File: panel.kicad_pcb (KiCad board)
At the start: 2 copper layers, 100 x 96.5 mm, 262 parts, among them J1 JST_SH_SM06B-SRSS-TB_1x06-1MP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, J2 JST_SH_SM04B-SRSS-TB_1x04-1MP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, J4 Conn_01x02, U1 M24C02-FMN

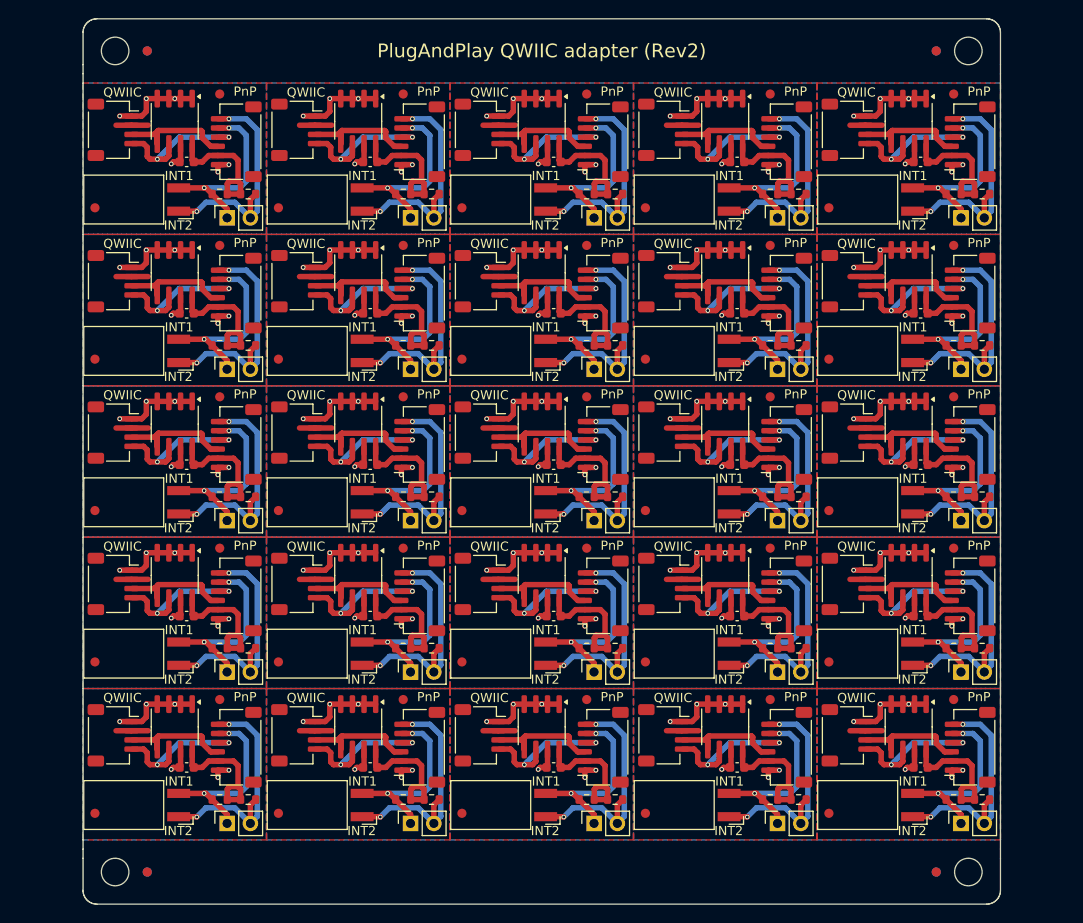
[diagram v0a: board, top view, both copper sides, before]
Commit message: Panel framing on all 4 sides
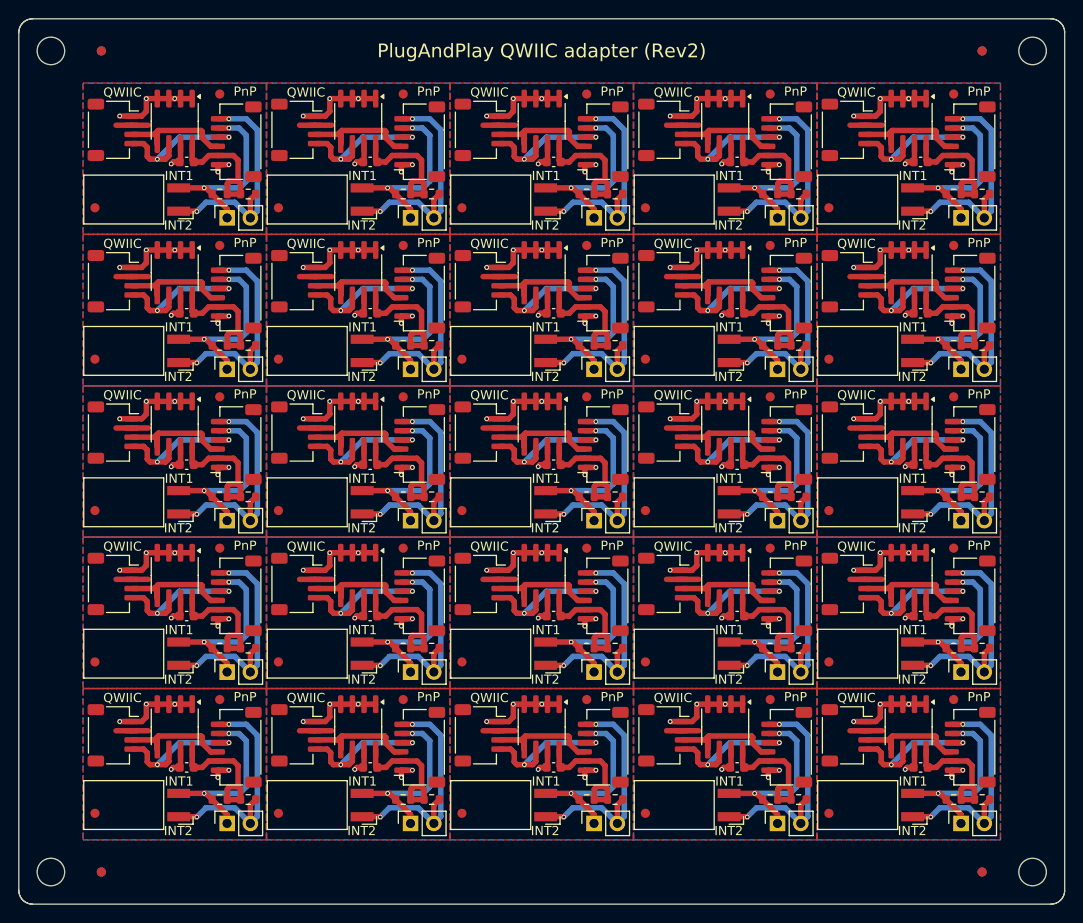
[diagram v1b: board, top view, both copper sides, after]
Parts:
- removed the C1 at (86.3, 101.6)
- removed the C1 at (66.3, 68.6)
- removed the C1 at (66.3, 35.6)
- removed the C1 at (86.3, 68.6)
- removed the C1 at (106.3, 85.1)
- removed the C1 at (86.3, 52.1)
- removed the C1 at (66.3, 101.6)
- removed the C1 at (106.3, 68.6)
- removed the C1 at (66.3, 85.1)
- removed the C1 at (126.3, 35.6)
- removed the C1 at (146.3, 85.1)
- removed the C1 at (86.3, 85.1)
- removed the C1 at (126.3, 101.6)
- removed the C1 at (66.3, 52.1)
- removed the C1 at (106.3, 35.6)
- removed the C1 at (106.3, 52.1)
- removed the C1 at (146.3, 35.6)
- removed the C1 at (126.3, 68.6)
- removed the C1 at (146.3, 52.1)
- removed the C1 at (106.3, 101.6)
- removed the C1 at (146.3, 101.6)
- removed the C1 at (126.3, 85.1)
- removed the C1 at (146.3, 68.6)
- removed the C1 at (126.3, 52.1)
- removed the C1 at (86.3, 35.6)
- removed the J1 at (131.7, 33.4)
- removed the J1 at (91.7, 82.9)
- removed the J1 at (131.7, 82.9)
- removed the J1 at (151.7, 82.9)
- removed the J1 at (131.7, 66.4)
- removed the J1 at (111.7, 99.4)
- removed the J1 at (151.7, 99.4)
- removed the J1 at (71.7, 33.4)
- removed the J1 at (71.7, 49.9)
- removed the J1 at (111.7, 82.9)
- removed the J1 at (71.7, 66.4)
- removed the J1 at (91.7, 66.4)
- removed the J1 at (151.7, 49.9)
- removed the J1 at (71.7, 82.9)
- removed the J1 at (151.7, 33.4)
- removed the J1 at (111.7, 49.9)
- removed the J1 at (111.7, 66.4)
- removed the J1 at (91.7, 33.4)
- removed the J1 at (91.7, 49.9)
- removed the J1 at (111.7, 33.4)
- removed the J1 at (131.7, 99.4)
- removed the J1 at (91.7, 99.4)
- removed the J1 at (151.7, 66.4)
- removed the J1 at (131.7, 49.9)
- removed the J1 at (71.7, 99.4)
- removed the J2 at (138.3, 98.1)
- removed the J2 at (98.3, 48.6)
- removed the J2 at (78.3, 81.6)
- removed the J2 at (78.3, 65.1)
- removed the J2 at (138.3, 48.6)
- removed the J2 at (58.3, 98.1)
- removed the J2 at (118.3, 32.1)
- removed the J2 at (138.3, 65.1)
- removed the J2 at (138.3, 81.6)
- removed the J2 at (118.3, 81.6)
- removed the J2 at (118.3, 65.1)
- removed the J2 at (98.3, 98.1)
- removed the J2 at (118.3, 98.1)
- removed the J2 at (58.3, 65.1)
- removed the J2 at (58.3, 81.6)
- removed the J2 at (98.3, 81.6)
- removed the J2 at (78.3, 48.6)
- removed the J2 at (58.3, 32.1)
- removed the J2 at (138.3, 32.1)
- removed the J2 at (78.3, 98.1)
- removed the J2 at (118.3, 48.6)
- removed the J2 at (58.3, 48.6)
- removed the J2 at (98.3, 32.1)
- removed the J2 at (78.3, 32.1)
- removed the J2 at (98.3, 65.1)
- removed the J3 at (79.9, 87.9)
- removed the J3 at (79.9, 54.9)
- removed the J3 at (139.9, 54.9)
- removed the J3 at (79.9, 104.4)
- removed the J3 at (59.9, 54.9)
- removed the J3 at (99.9, 38.4)
- removed the J3 at (99.9, 71.4)
- removed the J3 at (119.9, 54.9)
- removed the J3 at (119.9, 87.9)
- removed the J3 at (99.9, 54.9)
- removed the J3 at (59.9, 38.4)
- removed the J3 at (79.9, 71.4)
- removed the J3 at (139.9, 38.4)
- removed the J3 at (99.9, 104.4)
- removed the J3 at (139.9, 104.4)
- removed the J3 at (119.9, 104.4)
- removed the J3 at (59.9, 104.4)
- removed the J3 at (139.9, 87.9)
- removed the J3 at (119.9, 71.4)
- removed the J3 at (99.9, 87.9)
- removed the J3 at (59.9, 87.9)
- removed the J3 at (79.9, 38.4)
- removed the J3 at (59.9, 71.4)
- removed the J3 at (139.9, 71.4)
- removed the J3 at (119.9, 38.4)
- removed the J4 at (90.7, 41.7)
- removed the J4 at (70.7, 91.2)
- removed the J4 at (110.7, 41.7)
- removed the J4 at (70.7, 58.2)
- removed the J4 at (130.7, 41.7)
- removed the J4 at (150.7, 107.7)
- removed the J4 at (110.7, 58.2)
- removed the J4 at (110.7, 107.7)
- removed the J4 at (90.7, 74.7)
- removed the J4 at (70.7, 74.7)
- removed the J4 at (90.7, 58.2)
- removed the J4 at (130.7, 91.2)
- removed the J4 at (110.7, 91.2)
- removed the J4 at (150.7, 91.2)
- removed the J4 at (90.7, 107.7)
- removed the J4 at (110.7, 74.7)
- removed the J4 at (70.7, 107.7)
- removed the J4 at (90.7, 91.2)
- removed the J4 at (130.7, 58.2)
- removed the J4 at (130.7, 107.7)
- removed the J4 at (150.7, 41.7)
- removed the J4 at (70.7, 41.7)
- removed the J4 at (130.7, 74.7)
- removed the J4 at (150.7, 58.2)
- removed the J4 at (150.7, 74.7)
- removed the R1 at (113.0, 105.1)
- removed the R1 at (73.0, 105.1)
- removed the R1 at (93.0, 105.1)
- removed the R1 at (93.0, 55.6)
- removed the R1 at (93.0, 39.1)
- removed the R1 at (73.0, 88.6)
- removed the R1 at (73.0, 55.6)
- removed the R1 at (153.0, 88.6)
- removed the R1 at (93.0, 72.1)
- removed the R1 at (113.0, 88.6)
- removed the R1 at (133.0, 105.1)
- removed the R1 at (113.0, 72.1)
- removed the R1 at (153.0, 55.6)
- removed the R1 at (153.0, 105.1)
- removed the R1 at (153.0, 39.1)
- removed the R1 at (133.0, 72.1)
- removed the R1 at (153.0, 72.1)
- removed the R1 at (113.0, 39.1)
- removed the R1 at (133.0, 88.6)
- removed the R1 at (133.0, 39.1)
- removed the R1 at (133.0, 55.6)
- removed the R1 at (73.0, 72.1)
- removed the R1 at (113.0, 55.6)
- removed the R1 at (93.0, 88.6)
- removed the R1 at (73.0, 39.1)
- removed the R2 at (69.9, 72.1)
- removed the R2 at (109.9, 72.1)
- removed the R2 at (89.9, 72.1)
- removed the R2 at (69.9, 39.1)
- removed the R2 at (149.9, 72.1)
- removed the R2 at (129.9, 88.6)
- removed the R2 at (149.9, 105.1)
- removed the R2 at (89.9, 105.1)
- removed the R2 at (89.9, 88.6)
- removed the R2 at (69.9, 88.6)
- removed the R2 at (149.9, 39.1)
- removed the R2 at (129.9, 55.6)
- removed the R2 at (129.9, 105.1)
- removed the R2 at (109.9, 88.6)
- removed the R2 at (109.9, 105.1)
- removed the R2 at (89.9, 55.6)
- removed the R2 at (89.9, 39.1)
- removed the R2 at (69.9, 55.6)
- removed the R2 at (149.9, 55.6)
- removed the R2 at (149.9, 88.6)
- removed the R2 at (129.9, 39.1)
- removed the R2 at (109.9, 55.6)
- removed the R2 at (109.9, 39.1)
- removed the R2 at (69.9, 105.1)
- removed the R2 at (129.9, 72.1)
- removed the REF** at (116.3, 40.6)
- removed the REF** at (129.9, 61.2)
- removed the REF** at (96.3, 90.1)
- removed the REF** at (116.3, 90.1)
- removed the REF** at (76.3, 90.1)
- removed the REF** at (129.9, 44.7)
- removed the REF** at (96.3, 57.1)
- removed the REF** at (96.3, 73.6)
- removed the REF** at (56.3, 106.6)
- removed the REF** at (69.9, 28.2)
- removed the REF** at (116.3, 73.6)
- removed the REF** at (96.3, 106.6)
- removed the REF** at (69.9, 61.2)
- removed the REF** at (136.3, 106.6)
- removed the REF** at (56.3, 90.1)
- removed the REF** at (56.3, 57.1)
- removed the REF** at (76.3, 57.1)
- removed the REF** at (89.9, 94.2)
- removed the REF** at (109.9, 61.2)
- removed the REF** at (109.9, 77.7)
- removed the REF** at (136.3, 40.6)
- removed the REF** at (69.9, 94.2)
- removed the REF** at (76.3, 73.6)
- removed the REF** at (89.9, 77.7)
- removed the REF** at (76.3, 106.6)
- removed the REF** at (149.9, 61.2)
- removed the REF** at (89.9, 28.2)
- removed the REF** at (76.3, 40.6)
- removed the REF** at (136.3, 57.1)
- removed the REF** at (89.9, 44.7)
- removed the REF** at (56.3, 73.6)
- removed the REF** at (69.9, 44.7)
- removed the REF** at (129.9, 94.2)
- removed the REF** at (149.9, 94.2)
- removed the REF** at (149.9, 77.7)
- removed the REF** at (96.3, 40.6)
- removed the REF** at (129.9, 77.7)
- removed the REF** at (149.9, 44.7)
- removed the REF** at (109.9, 94.2)
- removed the REF** at (89.9, 61.2)
- removed the REF** at (56.3, 40.6)
- removed the REF** at (129.9, 28.2)
- removed the REF** at (116.3, 57.1)
- removed the REF** at (136.3, 90.1)
- removed the REF** at (116.3, 106.6)
- removed the REF** at (136.3, 73.6)
- removed the REF** at (109.9, 28.2)
- removed the REF** at (109.9, 44.7)
- removed the REF** at (69.9, 77.7)
- removed the REF** at (149.9, 28.2)
- removed the U1 at (145.0, 80.7)
- removed the U1 at (85.0, 97.2)
- removed the U1 at (125.0, 80.7)
- removed the U1 at (105.0, 47.7)
- removed the U1 at (125.0, 47.7)
- removed the U1 at (65.0, 80.7)
- removed the U1 at (145.0, 47.7)
- removed the U1 at (145.0, 64.2)
- removed the U1 at (145.0, 97.2)
- removed the U1 at (125.0, 31.2)
- removed the U1 at (105.0, 97.2)
- removed the U1 at (85.0, 31.2)
- removed the U1 at (105.0, 31.2)
- removed the U1 at (125.0, 97.2)
- removed the U1 at (85.0, 47.7)
- removed the U1 at (85.0, 64.2)
- removed the U1 at (85.0, 80.7)
- removed the U1 at (65.0, 97.2)
- removed the U1 at (65.0, 47.7)
- removed the U1 at (145.0, 31.2)
- removed the U1 at (65.0, 31.2)
- removed the U1 at (65.0, 64.2)
- removed the U1 at (105.0, 80.7)
- removed the U1 at (105.0, 64.2)
- removed the U1 at (125.0, 64.2)
- added C1: 0.1uF, Capacitor_SMD:C_0603_1608Metric, F.Cu at (86.3, 85.1)
- added C1: 0.1uF, Capacitor_SMD:C_0603_1608Metric, F.Cu at (106.3, 52.1)
- added C1: 0.1uF, Capacitor_SMD:C_0603_1608Metric, F.Cu at (146.3, 68.6)
- added C1: 0.1uF, Capacitor_SMD:C_0603_1608Metric, F.Cu at (126.3, 52.1)
- added C1: 0.1uF, Capacitor_SMD:C_0603_1608Metric, F.Cu at (146.3, 35.6)
- added C1: 0.1uF, Capacitor_SMD:C_0603_1608Metric, F.Cu at (106.3, 101.6)
- added C1: 0.1uF, Capacitor_SMD:C_0603_1608Metric, F.Cu at (126.3, 68.6)
- added C1: 0.1uF, Capacitor_SMD:C_0603_1608Metric, F.Cu at (146.3, 101.6)
- added C1: 0.1uF, Capacitor_SMD:C_0603_1608Metric, F.Cu at (146.3, 52.1)
- added C1: 0.1uF, Capacitor_SMD:C_0603_1608Metric, F.Cu at (106.3, 35.6)
- added C1: 0.1uF, Capacitor_SMD:C_0603_1608Metric, F.Cu at (86.3, 68.6)
- added C1: 0.1uF, Capacitor_SMD:C_0603_1608Metric, F.Cu at (66.3, 101.6)
- added C1: 0.1uF, Capacitor_SMD:C_0603_1608Metric, F.Cu at (66.3, 35.6)
- added C1: 0.1uF, Capacitor_SMD:C_0603_1608Metric, F.Cu at (86.3, 35.6)
- added C1: 0.1uF, Capacitor_SMD:C_0603_1608Metric, F.Cu at (66.3, 85.1)
- added C1: 0.1uF, Capacitor_SMD:C_0603_1608Metric, F.Cu at (126.3, 85.1)
- added C1: 0.1uF, Capacitor_SMD:C_0603_1608Metric, F.Cu at (86.3, 101.6)
- added C1: 0.1uF, Capacitor_SMD:C_0603_1608Metric, F.Cu at (106.3, 68.6)
- added C1: 0.1uF, Capacitor_SMD:C_0603_1608Metric, F.Cu at (66.3, 68.6)
- added C1: 0.1uF, Capacitor_SMD:C_0603_1608Metric, F.Cu at (146.3, 85.1)
- added C1: 0.1uF, Capacitor_SMD:C_0603_1608Metric, F.Cu at (126.3, 35.6)
- added C1: 0.1uF, Capacitor_SMD:C_0603_1608Metric, F.Cu at (66.3, 52.1)
- added C1: 0.1uF, Capacitor_SMD:C_0603_1608Metric, F.Cu at (126.3, 101.6)
- added C1: 0.1uF, Capacitor_SMD:C_0603_1608Metric, F.Cu at (86.3, 52.1)
- added C1: 0.1uF, Capacitor_SMD:C_0603_1608Metric, F.Cu at (106.3, 85.1)
- added J1: JST_SH_SM06B-SRSS-TB_1x06-1MP_P1.00mm_Horizontal, Connector_JST:JST_SH_SM06B-SRSS-TB_1x06-1MP_P1.00mm_Horizontal, F.Cu at (91.7, 66.4)
- added J1: JST_SH_SM06B-SRSS-TB_1x06-1MP_P1.00mm_Horizontal, Connector_JST:JST_SH_SM06B-SRSS-TB_1x06-1MP_P1.00mm_Horizontal, F.Cu at (111.7, 66.4)
- added J1: JST_SH_SM06B-SRSS-TB_1x06-1MP_P1.00mm_Horizontal, Connector_JST:JST_SH_SM06B-SRSS-TB_1x06-1MP_P1.00mm_Horizontal, F.Cu at (111.7, 33.4)
- added J1: JST_SH_SM06B-SRSS-TB_1x06-1MP_P1.00mm_Horizontal, Connector_JST:JST_SH_SM06B-SRSS-TB_1x06-1MP_P1.00mm_Horizontal, F.Cu at (91.7, 99.4)
- added J1: JST_SH_SM06B-SRSS-TB_1x06-1MP_P1.00mm_Horizontal, Connector_JST:JST_SH_SM06B-SRSS-TB_1x06-1MP_P1.00mm_Horizontal, F.Cu at (131.7, 49.9)
- added J1: JST_SH_SM06B-SRSS-TB_1x06-1MP_P1.00mm_Horizontal, Connector_JST:JST_SH_SM06B-SRSS-TB_1x06-1MP_P1.00mm_Horizontal, F.Cu at (131.7, 82.9)
- added J1: JST_SH_SM06B-SRSS-TB_1x06-1MP_P1.00mm_Horizontal, Connector_JST:JST_SH_SM06B-SRSS-TB_1x06-1MP_P1.00mm_Horizontal, F.Cu at (111.7, 82.9)
- added J1: JST_SH_SM06B-SRSS-TB_1x06-1MP_P1.00mm_Horizontal, Connector_JST:JST_SH_SM06B-SRSS-TB_1x06-1MP_P1.00mm_Horizontal, F.Cu at (91.7, 82.9)
- added J1: JST_SH_SM06B-SRSS-TB_1x06-1MP_P1.00mm_Horizontal, Connector_JST:JST_SH_SM06B-SRSS-TB_1x06-1MP_P1.00mm_Horizontal, F.Cu at (111.7, 49.9)
- added J1: JST_SH_SM06B-SRSS-TB_1x06-1MP_P1.00mm_Horizontal, Connector_JST:JST_SH_SM06B-SRSS-TB_1x06-1MP_P1.00mm_Horizontal, F.Cu at (71.7, 99.4)
- added J1: JST_SH_SM06B-SRSS-TB_1x06-1MP_P1.00mm_Horizontal, Connector_JST:JST_SH_SM06B-SRSS-TB_1x06-1MP_P1.00mm_Horizontal, F.Cu at (151.7, 82.9)
- added J1: JST_SH_SM06B-SRSS-TB_1x06-1MP_P1.00mm_Horizontal, Connector_JST:JST_SH_SM06B-SRSS-TB_1x06-1MP_P1.00mm_Horizontal, F.Cu at (151.7, 99.4)
- added J1: JST_SH_SM06B-SRSS-TB_1x06-1MP_P1.00mm_Horizontal, Connector_JST:JST_SH_SM06B-SRSS-TB_1x06-1MP_P1.00mm_Horizontal, F.Cu at (131.7, 66.4)
- added J1: JST_SH_SM06B-SRSS-TB_1x06-1MP_P1.00mm_Horizontal, Connector_JST:JST_SH_SM06B-SRSS-TB_1x06-1MP_P1.00mm_Horizontal, F.Cu at (91.7, 33.4)
- added J1: JST_SH_SM06B-SRSS-TB_1x06-1MP_P1.00mm_Horizontal, Connector_JST:JST_SH_SM06B-SRSS-TB_1x06-1MP_P1.00mm_Horizontal, F.Cu at (151.7, 49.9)
- added J1: JST_SH_SM06B-SRSS-TB_1x06-1MP_P1.00mm_Horizontal, Connector_JST:JST_SH_SM06B-SRSS-TB_1x06-1MP_P1.00mm_Horizontal, F.Cu at (71.7, 82.9)
- added J1: JST_SH_SM06B-SRSS-TB_1x06-1MP_P1.00mm_Horizontal, Connector_JST:JST_SH_SM06B-SRSS-TB_1x06-1MP_P1.00mm_Horizontal, F.Cu at (71.7, 49.9)
- added J1: JST_SH_SM06B-SRSS-TB_1x06-1MP_P1.00mm_Horizontal, Connector_JST:JST_SH_SM06B-SRSS-TB_1x06-1MP_P1.00mm_Horizontal, F.Cu at (71.7, 33.4)
- added J1: JST_SH_SM06B-SRSS-TB_1x06-1MP_P1.00mm_Horizontal, Connector_JST:JST_SH_SM06B-SRSS-TB_1x06-1MP_P1.00mm_Horizontal, F.Cu at (131.7, 99.4)
- added J1: JST_SH_SM06B-SRSS-TB_1x06-1MP_P1.00mm_Horizontal, Connector_JST:JST_SH_SM06B-SRSS-TB_1x06-1MP_P1.00mm_Horizontal, F.Cu at (71.7, 66.4)
- added J1: JST_SH_SM06B-SRSS-TB_1x06-1MP_P1.00mm_Horizontal, Connector_JST:JST_SH_SM06B-SRSS-TB_1x06-1MP_P1.00mm_Horizontal, F.Cu at (91.7, 49.9)
- added J1: JST_SH_SM06B-SRSS-TB_1x06-1MP_P1.00mm_Horizontal, Connector_JST:JST_SH_SM06B-SRSS-TB_1x06-1MP_P1.00mm_Horizontal, F.Cu at (151.7, 66.4)
- added J1: JST_SH_SM06B-SRSS-TB_1x06-1MP_P1.00mm_Horizontal, Connector_JST:JST_SH_SM06B-SRSS-TB_1x06-1MP_P1.00mm_Horizontal, F.Cu at (151.7, 33.4)
- added J1: JST_SH_SM06B-SRSS-TB_1x06-1MP_P1.00mm_Horizontal, Connector_JST:JST_SH_SM06B-SRSS-TB_1x06-1MP_P1.00mm_Horizontal, F.Cu at (111.7, 99.4)
- added J1: JST_SH_SM06B-SRSS-TB_1x06-1MP_P1.00mm_Horizontal, Connector_JST:JST_SH_SM06B-SRSS-TB_1x06-1MP_P1.00mm_Horizontal, F.Cu at (131.7, 33.4)
- added J2: JST_SH_SM04B-SRSS-TB_1x04-1MP_P1.00mm_Horizontal, Connector_JST:JST_SH_SM04B-SRSS-TB_1x04-1MP_P1.00mm_Horizontal, F.Cu at (138.3, 32.1)
- added J2: JST_SH_SM04B-SRSS-TB_1x04-1MP_P1.00mm_Horizontal, Connector_JST:JST_SH_SM04B-SRSS-TB_1x04-1MP_P1.00mm_Horizontal, F.Cu at (58.3, 65.1)
- added J2: JST_SH_SM04B-SRSS-TB_1x04-1MP_P1.00mm_Horizontal, Connector_JST:JST_SH_SM04B-SRSS-TB_1x04-1MP_P1.00mm_Horizontal, F.Cu at (138.3, 81.6)
- added J2: JST_SH_SM04B-SRSS-TB_1x04-1MP_P1.00mm_Horizontal, Connector_JST:JST_SH_SM04B-SRSS-TB_1x04-1MP_P1.00mm_Horizontal, F.Cu at (98.3, 48.6)
- added J2: JST_SH_SM04B-SRSS-TB_1x04-1MP_P1.00mm_Horizontal, Connector_JST:JST_SH_SM04B-SRSS-TB_1x04-1MP_P1.00mm_Horizontal, F.Cu at (138.3, 98.1)
- added J2: JST_SH_SM04B-SRSS-TB_1x04-1MP_P1.00mm_Horizontal, Connector_JST:JST_SH_SM04B-SRSS-TB_1x04-1MP_P1.00mm_Horizontal, F.Cu at (118.3, 81.6)
- added J2: JST_SH_SM04B-SRSS-TB_1x04-1MP_P1.00mm_Horizontal, Connector_JST:JST_SH_SM04B-SRSS-TB_1x04-1MP_P1.00mm_Horizontal, F.Cu at (98.3, 81.6)
- added J2: JST_SH_SM04B-SRSS-TB_1x04-1MP_P1.00mm_Horizontal, Connector_JST:JST_SH_SM04B-SRSS-TB_1x04-1MP_P1.00mm_Horizontal, F.Cu at (98.3, 98.1)
- added J2: JST_SH_SM04B-SRSS-TB_1x04-1MP_P1.00mm_Horizontal, Connector_JST:JST_SH_SM04B-SRSS-TB_1x04-1MP_P1.00mm_Horizontal, F.Cu at (98.3, 65.1)
- added J2: JST_SH_SM04B-SRSS-TB_1x04-1MP_P1.00mm_Horizontal, Connector_JST:JST_SH_SM04B-SRSS-TB_1x04-1MP_P1.00mm_Horizontal, F.Cu at (138.3, 65.1)
- added J2: JST_SH_SM04B-SRSS-TB_1x04-1MP_P1.00mm_Horizontal, Connector_JST:JST_SH_SM04B-SRSS-TB_1x04-1MP_P1.00mm_Horizontal, F.Cu at (78.3, 32.1)
- added J2: JST_SH_SM04B-SRSS-TB_1x04-1MP_P1.00mm_Horizontal, Connector_JST:JST_SH_SM04B-SRSS-TB_1x04-1MP_P1.00mm_Horizontal, F.Cu at (98.3, 32.1)
- added J2: JST_SH_SM04B-SRSS-TB_1x04-1MP_P1.00mm_Horizontal, Connector_JST:JST_SH_SM04B-SRSS-TB_1x04-1MP_P1.00mm_Horizontal, F.Cu at (58.3, 32.1)
- added J2: JST_SH_SM04B-SRSS-TB_1x04-1MP_P1.00mm_Horizontal, Connector_JST:JST_SH_SM04B-SRSS-TB_1x04-1MP_P1.00mm_Horizontal, F.Cu at (78.3, 65.1)
- added J2: JST_SH_SM04B-SRSS-TB_1x04-1MP_P1.00mm_Horizontal, Connector_JST:JST_SH_SM04B-SRSS-TB_1x04-1MP_P1.00mm_Horizontal, F.Cu at (78.3, 48.6)
- added J2: JST_SH_SM04B-SRSS-TB_1x04-1MP_P1.00mm_Horizontal, Connector_JST:JST_SH_SM04B-SRSS-TB_1x04-1MP_P1.00mm_Horizontal, F.Cu at (118.3, 48.6)
- added J2: JST_SH_SM04B-SRSS-TB_1x04-1MP_P1.00mm_Horizontal, Connector_JST:JST_SH_SM04B-SRSS-TB_1x04-1MP_P1.00mm_Horizontal, F.Cu at (58.3, 98.1)
- added J2: JST_SH_SM04B-SRSS-TB_1x04-1MP_P1.00mm_Horizontal, Connector_JST:JST_SH_SM04B-SRSS-TB_1x04-1MP_P1.00mm_Horizontal, F.Cu at (118.3, 65.1)
- added J2: JST_SH_SM04B-SRSS-TB_1x04-1MP_P1.00mm_Horizontal, Connector_JST:JST_SH_SM04B-SRSS-TB_1x04-1MP_P1.00mm_Horizontal, F.Cu at (78.3, 81.6)
- added J2: JST_SH_SM04B-SRSS-TB_1x04-1MP_P1.00mm_Horizontal, Connector_JST:JST_SH_SM04B-SRSS-TB_1x04-1MP_P1.00mm_Horizontal, F.Cu at (78.3, 98.1)
- added J2: JST_SH_SM04B-SRSS-TB_1x04-1MP_P1.00mm_Horizontal, Connector_JST:JST_SH_SM04B-SRSS-TB_1x04-1MP_P1.00mm_Horizontal, F.Cu at (118.3, 98.1)
- added J2: JST_SH_SM04B-SRSS-TB_1x04-1MP_P1.00mm_Horizontal, Connector_JST:JST_SH_SM04B-SRSS-TB_1x04-1MP_P1.00mm_Horizontal, F.Cu at (138.3, 48.6)
- added J2: JST_SH_SM04B-SRSS-TB_1x04-1MP_P1.00mm_Horizontal, Connector_JST:JST_SH_SM04B-SRSS-TB_1x04-1MP_P1.00mm_Horizontal, F.Cu at (118.3, 32.1)
- added J2: JST_SH_SM04B-SRSS-TB_1x04-1MP_P1.00mm_Horizontal, Connector_JST:JST_SH_SM04B-SRSS-TB_1x04-1MP_P1.00mm_Horizontal, F.Cu at (58.3, 48.6)
- added J2: JST_SH_SM04B-SRSS-TB_1x04-1MP_P1.00mm_Horizontal, Connector_JST:JST_SH_SM04B-SRSS-TB_1x04-1MP_P1.00mm_Horizontal, F.Cu at (58.3, 81.6)
- added J3: ~, Library:PinHeader_1x02_P2.54mm_Horizontal_SMD, F.Cu at (79.9, 54.9)
- added J3: ~, Library:PinHeader_1x02_P2.54mm_Horizontal_SMD, F.Cu at (139.9, 104.4)
- added J3: ~, Library:PinHeader_1x02_P2.54mm_Horizontal_SMD, F.Cu at (119.9, 54.9)
- added J3: ~, Library:PinHeader_1x02_P2.54mm_Horizontal_SMD, F.Cu at (59.9, 38.4)
- added J3: ~, Library:PinHeader_1x02_P2.54mm_Horizontal_SMD, F.Cu at (99.9, 104.4)
- added J3: ~, Library:PinHeader_1x02_P2.54mm_Horizontal_SMD, F.Cu at (99.9, 71.4)
- added J3: ~, Library:PinHeader_1x02_P2.54mm_Horizontal_SMD, F.Cu at (79.9, 104.4)
- added J3: ~, Library:PinHeader_1x02_P2.54mm_Horizontal_SMD, F.Cu at (99.9, 87.9)
- added J3: ~, Library:PinHeader_1x02_P2.54mm_Horizontal_SMD, F.Cu at (139.9, 38.4)
- added J3: ~, Library:PinHeader_1x02_P2.54mm_Horizontal_SMD, F.Cu at (59.9, 54.9)
- added J3: ~, Library:PinHeader_1x02_P2.54mm_Horizontal_SMD, F.Cu at (59.9, 71.4)
- added J3: ~, Library:PinHeader_1x02_P2.54mm_Horizontal_SMD, F.Cu at (119.9, 87.9)
- added J3: ~, Library:PinHeader_1x02_P2.54mm_Horizontal_SMD, F.Cu at (119.9, 38.4)
- added J3: ~, Library:PinHeader_1x02_P2.54mm_Horizontal_SMD, F.Cu at (59.9, 87.9)
- added J3: ~, Library:PinHeader_1x02_P2.54mm_Horizontal_SMD, F.Cu at (139.9, 54.9)
- added J3: ~, Library:PinHeader_1x02_P2.54mm_Horizontal_SMD, F.Cu at (79.9, 71.4)
- added J3: ~, Library:PinHeader_1x02_P2.54mm_Horizontal_SMD, F.Cu at (99.9, 38.4)
- added J3: ~, Library:PinHeader_1x02_P2.54mm_Horizontal_SMD, F.Cu at (99.9, 54.9)
- added J3: ~, Library:PinHeader_1x02_P2.54mm_Horizontal_SMD, F.Cu at (79.9, 87.9)
- added J3: ~, Library:PinHeader_1x02_P2.54mm_Horizontal_SMD, F.Cu at (79.9, 38.4)
- added J3: ~, Library:PinHeader_1x02_P2.54mm_Horizontal_SMD, F.Cu at (119.9, 71.4)
- added J3: ~, Library:PinHeader_1x02_P2.54mm_Horizontal_SMD, F.Cu at (119.9, 104.4)
- added J3: ~, Library:PinHeader_1x02_P2.54mm_Horizontal_SMD, F.Cu at (139.9, 87.9)
- added J3: ~, Library:PinHeader_1x02_P2.54mm_Horizontal_SMD, F.Cu at (139.9, 71.4)
- added J3: ~, Library:PinHeader_1x02_P2.54mm_Horizontal_SMD, F.Cu at (59.9, 104.4)
- added J4: Conn_01x02, Connector_PinSocket_2.54mm:PinSocket_1x02_P2.54mm_Vertical, F.Cu at (110.7, 58.2)
- added J4: Conn_01x02, Connector_PinSocket_2.54mm:PinSocket_1x02_P2.54mm_Vertical, F.Cu at (90.7, 58.2)
- added J4: Conn_01x02, Connector_PinSocket_2.54mm:PinSocket_1x02_P2.54mm_Vertical, F.Cu at (130.7, 91.2)
- added J4: Conn_01x02, Connector_PinSocket_2.54mm:PinSocket_1x02_P2.54mm_Vertical, F.Cu at (90.7, 74.7)
- added J4: Conn_01x02, Connector_PinSocket_2.54mm:PinSocket_1x02_P2.54mm_Vertical, F.Cu at (90.7, 41.7)
- added J4: Conn_01x02, Connector_PinSocket_2.54mm:PinSocket_1x02_P2.54mm_Vertical, F.Cu at (70.7, 91.2)
- added J4: Conn_01x02, Connector_PinSocket_2.54mm:PinSocket_1x02_P2.54mm_Vertical, F.Cu at (110.7, 107.7)
- added J4: Conn_01x02, Connector_PinSocket_2.54mm:PinSocket_1x02_P2.54mm_Vertical, F.Cu at (150.7, 107.7)
- added J4: Conn_01x02, Connector_PinSocket_2.54mm:PinSocket_1x02_P2.54mm_Vertical, F.Cu at (150.7, 91.2)
- added J4: Conn_01x02, Connector_PinSocket_2.54mm:PinSocket_1x02_P2.54mm_Vertical, F.Cu at (70.7, 74.7)
- added J4: Conn_01x02, Connector_PinSocket_2.54mm:PinSocket_1x02_P2.54mm_Vertical, F.Cu at (70.7, 107.7)
- added J4: Conn_01x02, Connector_PinSocket_2.54mm:PinSocket_1x02_P2.54mm_Vertical, F.Cu at (110.7, 91.2)
- added J4: Conn_01x02, Connector_PinSocket_2.54mm:PinSocket_1x02_P2.54mm_Vertical, F.Cu at (110.7, 74.7)
- added J4: Conn_01x02, Connector_PinSocket_2.54mm:PinSocket_1x02_P2.54mm_Vertical, F.Cu at (130.7, 74.7)
- added J4: Conn_01x02, Connector_PinSocket_2.54mm:PinSocket_1x02_P2.54mm_Vertical, F.Cu at (130.7, 41.7)
- added J4: Conn_01x02, Connector_PinSocket_2.54mm:PinSocket_1x02_P2.54mm_Vertical, F.Cu at (130.7, 107.7)
- added J4: Conn_01x02, Connector_PinSocket_2.54mm:PinSocket_1x02_P2.54mm_Vertical, F.Cu at (90.7, 91.2)
- added J4: Conn_01x02, Connector_PinSocket_2.54mm:PinSocket_1x02_P2.54mm_Vertical, F.Cu at (70.7, 58.2)
- added J4: Conn_01x02, Connector_PinSocket_2.54mm:PinSocket_1x02_P2.54mm_Vertical, F.Cu at (150.7, 41.7)
- added J4: Conn_01x02, Connector_PinSocket_2.54mm:PinSocket_1x02_P2.54mm_Vertical, F.Cu at (150.7, 74.7)
- added J4: Conn_01x02, Connector_PinSocket_2.54mm:PinSocket_1x02_P2.54mm_Vertical, F.Cu at (70.7, 41.7)
- added J4: Conn_01x02, Connector_PinSocket_2.54mm:PinSocket_1x02_P2.54mm_Vertical, F.Cu at (110.7, 41.7)
- added J4: Conn_01x02, Connector_PinSocket_2.54mm:PinSocket_1x02_P2.54mm_Vertical, F.Cu at (90.7, 107.7)
- added J4: Conn_01x02, Connector_PinSocket_2.54mm:PinSocket_1x02_P2.54mm_Vertical, F.Cu at (130.7, 58.2)
- added J4: Conn_01x02, Connector_PinSocket_2.54mm:PinSocket_1x02_P2.54mm_Vertical, F.Cu at (150.7, 58.2)
- added R1: 10K, Resistor_SMD:R_0603_1608Metric, F.Cu at (113.0, 105.1)
- added R1: 10K, Resistor_SMD:R_0603_1608Metric, F.Cu at (73.0, 39.1)
- added R1: 10K, Resistor_SMD:R_0603_1608Metric, F.Cu at (93.0, 55.6)
- added R1: 10K, Resistor_SMD:R_0603_1608Metric, F.Cu at (73.0, 88.6)
- added R1: 10K, Resistor_SMD:R_0603_1608Metric, F.Cu at (153.0, 55.6)
- added R1: 10K, Resistor_SMD:R_0603_1608Metric, F.Cu at (113.0, 55.6)
- added R1: 10K, Resistor_SMD:R_0603_1608Metric, F.Cu at (73.0, 72.1)
- added R1: 10K, Resistor_SMD:R_0603_1608Metric, F.Cu at (153.0, 72.1)
- added R1: 10K, Resistor_SMD:R_0603_1608Metric, F.Cu at (113.0, 88.6)
- added R1: 10K, Resistor_SMD:R_0603_1608Metric, F.Cu at (113.0, 72.1)
- added R1: 10K, Resistor_SMD:R_0603_1608Metric, F.Cu at (133.0, 39.1)
- added R1: 10K, Resistor_SMD:R_0603_1608Metric, F.Cu at (153.0, 88.6)
- added R1: 10K, Resistor_SMD:R_0603_1608Metric, F.Cu at (133.0, 72.1)
- added R1: 10K, Resistor_SMD:R_0603_1608Metric, F.Cu at (133.0, 55.6)
- added R1: 10K, Resistor_SMD:R_0603_1608Metric, F.Cu at (73.0, 105.1)
- added R1: 10K, Resistor_SMD:R_0603_1608Metric, F.Cu at (73.0, 55.6)
- added R1: 10K, Resistor_SMD:R_0603_1608Metric, F.Cu at (93.0, 72.1)
- added R1: 10K, Resistor_SMD:R_0603_1608Metric, F.Cu at (93.0, 88.6)
- added R1: 10K, Resistor_SMD:R_0603_1608Metric, F.Cu at (93.0, 39.1)
- added R1: 10K, Resistor_SMD:R_0603_1608Metric, F.Cu at (93.0, 105.1)
- added R1: 10K, Resistor_SMD:R_0603_1608Metric, F.Cu at (153.0, 39.1)
- added R1: 10K, Resistor_SMD:R_0603_1608Metric, F.Cu at (133.0, 105.1)
- added R1: 10K, Resistor_SMD:R_0603_1608Metric, F.Cu at (113.0, 39.1)
- added R1: 10K, Resistor_SMD:R_0603_1608Metric, F.Cu at (153.0, 105.1)
- added R1: 10K, Resistor_SMD:R_0603_1608Metric, F.Cu at (133.0, 88.6)
- added R2: 10K, Resistor_SMD:R_0603_1608Metric, F.Cu at (109.9, 88.6)
- added R2: 10K, Resistor_SMD:R_0603_1608Metric, F.Cu at (149.9, 39.1)
- added R2: 10K, Resistor_SMD:R_0603_1608Metric, F.Cu at (149.9, 88.6)
- added R2: 10K, Resistor_SMD:R_0603_1608Metric, F.Cu at (69.9, 88.6)
- added R2: 10K, Resistor_SMD:R_0603_1608Metric, F.Cu at (69.9, 105.1)
- added R2: 10K, Resistor_SMD:R_0603_1608Metric, F.Cu at (129.9, 105.1)
- added R2: 10K, Resistor_SMD:R_0603_1608Metric, F.Cu at (129.9, 39.1)
- added R2: 10K, Resistor_SMD:R_0603_1608Metric, F.Cu at (89.9, 105.1)
- added R2: 10K, Resistor_SMD:R_0603_1608Metric, F.Cu at (129.9, 88.6)
- added R2: 10K, Resistor_SMD:R_0603_1608Metric, F.Cu at (89.9, 55.6)
- added R2: 10K, Resistor_SMD:R_0603_1608Metric, F.Cu at (149.9, 55.6)
- added R2: 10K, Resistor_SMD:R_0603_1608Metric, F.Cu at (149.9, 72.1)
- added R2: 10K, Resistor_SMD:R_0603_1608Metric, F.Cu at (109.9, 39.1)
- added R2: 10K, Resistor_SMD:R_0603_1608Metric, F.Cu at (89.9, 39.1)
- added R2: 10K, Resistor_SMD:R_0603_1608Metric, F.Cu at (69.9, 55.6)
- added R2: 10K, Resistor_SMD:R_0603_1608Metric, F.Cu at (129.9, 55.6)
- added R2: 10K, Resistor_SMD:R_0603_1608Metric, F.Cu at (109.9, 55.6)
- added R2: 10K, Resistor_SMD:R_0603_1608Metric, F.Cu at (109.9, 72.1)
- added R2: 10K, Resistor_SMD:R_0603_1608Metric, F.Cu at (129.9, 72.1)
- added R2: 10K, Resistor_SMD:R_0603_1608Metric, F.Cu at (69.9, 39.1)
- added R2: 10K, Resistor_SMD:R_0603_1608Metric, F.Cu at (149.9, 105.1)
- added R2: 10K, Resistor_SMD:R_0603_1608Metric, F.Cu at (69.9, 72.1)
- added R2: 10K, Resistor_SMD:R_0603_1608Metric, F.Cu at (109.9, 105.1)
- added R2: 10K, Resistor_SMD:R_0603_1608Metric, F.Cu at (89.9, 88.6)
- added R2: 10K, Resistor_SMD:R_0603_1608Metric, F.Cu at (89.9, 72.1)
- added REF**: Fiducial_1mm_Mask2mm, Fiducial:Fiducial_1mm_Mask2mm, F.Cu at (149.9, 61.2)
- added REF**: Fiducial_1mm_Mask2mm, Fiducial:Fiducial_1mm_Mask2mm, F.Cu at (136.3, 106.6)
- added REF**: Fiducial_1mm_Mask2mm, Fiducial:Fiducial_1mm_Mask2mm, F.Cu at (76.3, 106.6)
- added REF**: Fiducial_1mm_Mask2mm, Fiducial:Fiducial_1mm_Mask2mm, F.Cu at (149.9, 44.7)
- added REF**: Fiducial_1mm_Mask2mm, Fiducial:Fiducial_1mm_Mask2mm, F.Cu at (76.3, 90.1)
- added REF**: Fiducial_1mm_Mask2mm, Fiducial:Fiducial_1mm_Mask2mm, F.Cu at (129.9, 77.7)
- added REF**: Fiducial_1mm_Mask2mm, Fiducial:Fiducial_1mm_Mask2mm, F.Cu at (109.9, 44.7)
- added REF**: Fiducial_1mm_Mask2mm, Fiducial:Fiducial_1mm_Mask2mm, F.Cu at (129.9, 44.7)
- added REF**: Fiducial_1mm_Mask2mm, Fiducial:Fiducial_1mm_Mask2mm, F.Cu at (96.3, 73.6)
- added REF**: Fiducial_1mm_Mask2mm, Fiducial:Fiducial_1mm_Mask2mm, F.Cu at (116.3, 57.1)
- added REF**: Fiducial_1mm_Mask2mm, Fiducial:Fiducial_1mm_Mask2mm, F.Cu at (109.9, 61.2)
- added REF**: Fiducial_1mm_Mask2mm, Fiducial:Fiducial_1mm_Mask2mm, F.Cu at (149.9, 77.7)
- added REF**: Fiducial_1mm_Mask2mm, Fiducial:Fiducial_1mm_Mask2mm, F.Cu at (136.3, 90.1)
- added REF**: Fiducial_1mm_Mask2mm, Fiducial:Fiducial_1mm_Mask2mm, F.Cu at (56.3, 57.1)
- added REF**: Fiducial_1mm_Mask2mm, Fiducial:Fiducial_1mm_Mask2mm, F.Cu at (149.9, 28.2)
- added REF**: Fiducial_1mm_Mask2mm, Fiducial:Fiducial_1mm_Mask2mm, F.Cu at (69.9, 94.2)
- added REF**: Fiducial_1mm_Mask2mm, Fiducial:Fiducial_1mm_Mask2mm, F.Cu at (136.3, 57.1)
- added REF**: Fiducial_1mm_Mask2mm, Fiducial:Fiducial_1mm_Mask2mm, F.Cu at (69.9, 44.7)
- added REF**: Fiducial_1mm_Mask2mm, Fiducial:Fiducial_1mm_Mask2mm, F.Cu at (149.9, 94.2)
- added REF**: Fiducial_1mm_Mask2mm, Fiducial:Fiducial_1mm_Mask2mm, F.Cu at (96.3, 90.1)
- added REF**: Fiducial_1mm_Mask2mm, Fiducial:Fiducial_1mm_Mask2mm, F.Cu at (69.9, 28.2)
- added REF**: Fiducial_1mm_Mask2mm, Fiducial:Fiducial_1mm_Mask2mm, F.Cu at (89.9, 28.2)
- added REF**: Fiducial_1mm_Mask2mm, Fiducial:Fiducial_1mm_Mask2mm, F.Cu at (76.3, 57.1)
- added REF**: Fiducial_1mm_Mask2mm, Fiducial:Fiducial_1mm_Mask2mm, F.Cu at (116.3, 40.6)
- added REF**: Fiducial_1mm_Mask2mm, Fiducial:Fiducial_1mm_Mask2mm, F.Cu at (89.9, 77.7)
- added REF**: Fiducial_1mm_Mask2mm, Fiducial:Fiducial_1mm_Mask2mm, F.Cu at (56.3, 106.6)
- added REF**: Fiducial_1mm_Mask2mm, Fiducial:Fiducial_1mm_Mask2mm, F.Cu at (116.3, 106.6)
- added REF**: Fiducial_1mm_Mask2mm, Fiducial:Fiducial_1mm_Mask2mm, F.Cu at (96.3, 106.6)
- added REF**: Fiducial_1mm_Mask2mm, Fiducial:Fiducial_1mm_Mask2mm, F.Cu at (89.9, 94.2)
- added REF**: Fiducial_1mm_Mask2mm, Fiducial:Fiducial_1mm_Mask2mm, F.Cu at (56.3, 73.6)
- added REF**: Fiducial_1mm_Mask2mm, Fiducial:Fiducial_1mm_Mask2mm, F.Cu at (109.9, 94.2)
- added REF**: Fiducial_1mm_Mask2mm, Fiducial:Fiducial_1mm_Mask2mm, F.Cu at (136.3, 73.6)
- added REF**: Fiducial_1mm_Mask2mm, Fiducial:Fiducial_1mm_Mask2mm, F.Cu at (89.9, 44.7)
- added REF**: Fiducial_1mm_Mask2mm, Fiducial:Fiducial_1mm_Mask2mm, F.Cu at (69.9, 61.2)
- added REF**: Fiducial_1mm_Mask2mm, Fiducial:Fiducial_1mm_Mask2mm, F.Cu at (69.9, 77.7)
- added REF**: Fiducial_1mm_Mask2mm, Fiducial:Fiducial_1mm_Mask2mm, F.Cu at (129.9, 61.2)
- added REF**: Fiducial_1mm_Mask2mm, Fiducial:Fiducial_1mm_Mask2mm, F.Cu at (109.9, 77.7)
- added REF**: Fiducial_1mm_Mask2mm, Fiducial:Fiducial_1mm_Mask2mm, F.Cu at (136.3, 40.6)
- added REF**: Fiducial_1mm_Mask2mm, Fiducial:Fiducial_1mm_Mask2mm, F.Cu at (116.3, 90.1)
- added REF**: Fiducial_1mm_Mask2mm, Fiducial:Fiducial_1mm_Mask2mm, F.Cu at (116.3, 73.6)
- added REF**: Fiducial_1mm_Mask2mm, Fiducial:Fiducial_1mm_Mask2mm, F.Cu at (129.9, 94.2)
- added REF**: Fiducial_1mm_Mask2mm, Fiducial:Fiducial_1mm_Mask2mm, F.Cu at (109.9, 28.2)
- added REF**: Fiducial_1mm_Mask2mm, Fiducial:Fiducial_1mm_Mask2mm, F.Cu at (89.9, 61.2)
- added REF**: Fiducial_1mm_Mask2mm, Fiducial:Fiducial_1mm_Mask2mm, F.Cu at (56.3, 40.6)
- added REF**: Fiducial_1mm_Mask2mm, Fiducial:Fiducial_1mm_Mask2mm, F.Cu at (129.9, 28.2)
- added REF**: Fiducial_1mm_Mask2mm, Fiducial:Fiducial_1mm_Mask2mm, F.Cu at (76.3, 40.6)
- added REF**: Fiducial_1mm_Mask2mm, Fiducial:Fiducial_1mm_Mask2mm, F.Cu at (96.3, 40.6)
- added REF**: Fiducial_1mm_Mask2mm, Fiducial:Fiducial_1mm_Mask2mm, F.Cu at (76.3, 73.6)
- added REF**: Fiducial_1mm_Mask2mm, Fiducial:Fiducial_1mm_Mask2mm, F.Cu at (56.3, 90.1)
- added REF**: Fiducial_1mm_Mask2mm, Fiducial:Fiducial_1mm_Mask2mm, F.Cu at (96.3, 57.1)
- added U1: M24C02-FMN, Package_SO:SOIC-8_3.9x4.9mm_P1.27mm, F.Cu at (145.0, 64.2)
- added U1: M24C02-FMN, Package_SO:SOIC-8_3.9x4.9mm_P1.27mm, F.Cu at (105.0, 47.7)
- added U1: M24C02-FMN, Package_SO:SOIC-8_3.9x4.9mm_P1.27mm, F.Cu at (85.0, 80.7)
- added U1: M24C02-FMN, Package_SO:SOIC-8_3.9x4.9mm_P1.27mm, F.Cu at (105.0, 31.2)
- added U1: M24C02-FMN, Package_SO:SOIC-8_3.9x4.9mm_P1.27mm, F.Cu at (125.0, 47.7)
- added U1: M24C02-FMN, Package_SO:SOIC-8_3.9x4.9mm_P1.27mm, F.Cu at (65.0, 80.7)
- added U1: M24C02-FMN, Package_SO:SOIC-8_3.9x4.9mm_P1.27mm, F.Cu at (85.0, 97.2)
- added U1: M24C02-FMN, Package_SO:SOIC-8_3.9x4.9mm_P1.27mm, F.Cu at (145.0, 47.7)
- added U1: M24C02-FMN, Package_SO:SOIC-8_3.9x4.9mm_P1.27mm, F.Cu at (105.0, 97.2)
- added U1: M24C02-FMN, Package_SO:SOIC-8_3.9x4.9mm_P1.27mm, F.Cu at (65.0, 97.2)
- added U1: M24C02-FMN, Package_SO:SOIC-8_3.9x4.9mm_P1.27mm, F.Cu at (145.0, 31.2)
- added U1: M24C02-FMN, Package_SO:SOIC-8_3.9x4.9mm_P1.27mm, F.Cu at (145.0, 80.7)
- added U1: M24C02-FMN, Package_SO:SOIC-8_3.9x4.9mm_P1.27mm, F.Cu at (125.0, 97.2)
- added U1: M24C02-FMN, Package_SO:SOIC-8_3.9x4.9mm_P1.27mm, F.Cu at (85.0, 64.2)
- added U1: M24C02-FMN, Package_SO:SOIC-8_3.9x4.9mm_P1.27mm, F.Cu at (105.0, 64.2)
- added U1: M24C02-FMN, Package_SO:SOIC-8_3.9x4.9mm_P1.27mm, F.Cu at (125.0, 64.2)
- added U1: M24C02-FMN, Package_SO:SOIC-8_3.9x4.9mm_P1.27mm, F.Cu at (85.0, 47.7)
- added U1: M24C02-FMN, Package_SO:SOIC-8_3.9x4.9mm_P1.27mm, F.Cu at (65.0, 47.7)
- added U1: M24C02-FMN, Package_SO:SOIC-8_3.9x4.9mm_P1.27mm, F.Cu at (85.0, 31.2)
- added U1: M24C02-FMN, Package_SO:SOIC-8_3.9x4.9mm_P1.27mm, F.Cu at (125.0, 80.7)
- added U1: M24C02-FMN, Package_SO:SOIC-8_3.9x4.9mm_P1.27mm, F.Cu at (65.0, 31.2)
- added U1: M24C02-FMN, Package_SO:SOIC-8_3.9x4.9mm_P1.27mm, F.Cu at (105.0, 80.7)
- added U1: M24C02-FMN, Package_SO:SOIC-8_3.9x4.9mm_P1.27mm, F.Cu at (125.0, 31.2)
- added U1: M24C02-FMN, Package_SO:SOIC-8_3.9x4.9mm_P1.27mm, F.Cu at (65.0, 64.2)
- added U1: M24C02-FMN, Package_SO:SOIC-8_3.9x4.9mm_P1.27mm, F.Cu at (145.0, 97.2)
- moved KiKit_TO_3 7.00 mm to (51.5, 113.0)
- moved KiKit_TO_4 7.00 mm to (158.5, 113.0)
- moved KiKit_TO_1 7.00 mm to (51.5, 23.5)
- moved KiKit_TO_2 7.00 mm to (158.5, 23.5)
- moved KiKit_FID_B_3 5.00 mm to (57.0, 113.0)
- moved KiKit_FID_B_4 5.00 mm to (153.0, 113.0)
- moved KiKit_FID_T_3 5.00 mm to (57.0, 113.0)
- moved KiKit_FID_T_4 5.00 mm to (153.0, 113.0)
- moved KiKit_FID_B_1 5.00 mm to (57.0, 23.5)
- moved KiKit_FID_B_2 5.00 mm to (153.0, 23.5)
- moved KiKit_FID_T_1 5.00 mm to (57.0, 23.5)
- moved KiKit_FID_T_2 5.00 mm to (153.0, 23.5)
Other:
- board size 100 x 96.5 mm -> 114 x 96.5 mm
